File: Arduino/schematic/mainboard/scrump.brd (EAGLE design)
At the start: 100 x 80 mm, 26 parts, among them J1 PINHEAD-FTSH, J2 USB-CON-5PIN-105017-0001, U1 ATSAMD21G-A, U2 LM3671, U3 MCP73831, Y1 32.768kHz

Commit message: Fixed issues after review - Missing 3.3V line on Vddana - Added decoupling cap for second vddio - Removed pull-up on swdclk, which is usually included in the programmer itself. - Added 22 ohm resistor in series with D+ and D-(USB) - Pin 9 of the SWD header is also GND
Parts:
- added C13: 0.1uF, SparkFun-Capacitors:0603-CAP
- added R5: 22R, SparkFun-Resistors:0603-RES
- R1: value 1K -> 22R
- moved R1 31.1 mm to (3.81, -7.62)
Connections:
- new net N$9: R1.1, U1.33
- net +3V3: now also C13.1, C2.1, C4.1, U1.6; no longer R1.2
- net D+: now also R5.2; no longer U1.34
- net D-: now also R1.2; no longer U1.33
- net GND: now also C13.2, J1.9
- net N$4: now also R5.1, U1.34; no longer C2.1, C4.1, U1.6
- net SWCLK: no longer R1.1
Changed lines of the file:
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@@
 <element name="C3" library="SparkFun-Capacitors" package="0603-CAP" value="1.0uF" x="22.86" y="11.43"/>
 <element name="C1" library="SparkFun-Capacitors" package="0603-CAP" value="0.1uF" x="10.16" y="16.51"/>
-<element name="R1" library="SparkFun-Resistors" package="0603-RES" value="1K" x="10.16" y="22.86"/>
 <element name="J2" library="mylibrary" package="USB-MICRO-MOLEX-105017-0001" value="USB-CON-5PIN-105017-0001" x="34.29" y="5.08"/>
 <element name="Y1" library="mylibrary" package="ABS25" value="32.768kHz" x="52.07" y="6.35"/>
@@
 <attribute name="PROD_ID" value="DIO-00819" x="54.61" y="19.05" size="1.778" layer="27" display="off"/>
 </element>
+<element name="C13" library="SparkFun-Capacitors" package="0603-CAP" value="0.1uF" x="3.81" y="-3.81"/>
+<element name="R1" library="SparkFun-Resistors" package="0603-RES" value="22R" x="3.81" y="-7.62"/>
+<element name="R5" library="SparkFun-Resistors" package="0603-RES" value="22R" x="3.81" y="-11.43"/>
 </elements>
 <signals>
@@
 <contactref element="U3" pad="2"/>
 <contactref element="R4" pad="1"/>
-<wire x1="44.45" y1="20.828" x2="53.76" y2="27.94" width="0" layer="19" extent="1-1"/>
+<contactref element="C13" pad="2"/>
+<contactref element="J1" pad="9"/>
+<wire x1="46.99" y1="20.828" x2="53.76" y2="27.94" width="0" layer="19" extent="1-1"/>
+<wire x1="44.45" y1="20.828" x2="46.99" y2="20.828" width="0" layer="19" extent="1-1"/>
 <wire x1="43.18" y1="20.828" x2="44.45" y2="20.828" width="0" layer="19" extent="1-1"/>
 <wire x1="36.83" y1="17.7499" x2="43.18" y2="20.828" width="0" layer="19" extent="1-1"/>
@@
 <wire x1="8.47" y1="2.54" x2="16.09" y2="2.54" width="0" layer="19" extent="1-1"/>
 <wire x1="8.47" y1="7.62" x2="8.47" y2="2.54" width="0" layer="19" extent="1-1"/>
+<wire x1="4.66" y1="-3.81" x2="8.47" y2="2.54" width="0" layer="19" extent="1-1"/>
 <wire x1="45.3" y1="12.7" x2="44.45" y2="20.828" width="0" layer="19" extent="1-1"/>
 <wire x1="42.76" y1="34.29" x2="53.76" y2="27.94" width="0" layer="19" extent="1-1"/>
 <wire x1="64.35" y1="10.16" x2="45.3" y2="12.7" width="0" layer="19" extent="1-1"/>
 <wire x1="69.43" y1="11.43" x2="64.35" y2="10.16" width="0" layer="19" extent="1-1"/>
-</signal>
-<signal name="N$4">
-<contactref element="U1" pad="6"/>
-<contactref element="C4" pad="1"/>
-<contactref element="C2" pad="1"/>
-<wire x1="20.74" y1="3.81" x2="14.8" y2="18.03" width="0" layer="19" extent="1-1"/>
-<wire x1="14.39" y1="2.54" x2="20.74" y2="3.81" width="0" layer="19" extent="1-1"/>
 </signal>
 <signal name="SWDIO">
@@
 <signal name="+3V3">
 <contactref element="U1" pad="17"/>
-<contactref element="U1" pad="36"/>
 <contactref element="U1" pad="44"/>
 <contactref element="J1" pad="1"/>
-<contactref element="R1" pad="2"/>
-<contactref element="C5" pad="1"/>
 <contactref element="C1" pad="1"/>
 <contactref element="C12" pad="1"/>
 <contactref element="U2" pad="4"/>
 <contactref element="L1" pad="1"/>
+<contactref element="U1" pad="6"/>
+<contactref element="C4" pad="1"/>
+<contactref element="C2" pad="1"/>
+<contactref element="C13" pad="1"/>
+<contactref element="U1" pad="36"/>
+<contactref element="C5" pad="1"/>
 <wire x1="37.78" y1="14.0001" x2="41.91" y2="20.828" width="0" layer="19" extent="1-1"/>
 <wire x1="43.6" y1="12.7" x2="37.78" y2="14.0001" width="0" layer="19" extent="1-1"/>
@@
 <wire x1="23.3" y1="20.53" x2="30.85" y2="12.7" width="0" layer="19" extent="1-1"/>
 <wire x1="18.3" y1="22.03" x2="23.3" y2="20.53" width="0" layer="19" extent="1-1"/>
-<wire x1="11.01" y1="22.86" x2="18.3" y2="22.03" width="0" layer="19" extent="1-1"/>
-<wire x1="9.31" y1="16.51" x2="11.01" y2="22.86" width="0" layer="19" extent="1-1"/>
-<wire x1="18.3" y1="13.53" x2="18.3" y2="22.03" width="0" layer="19" extent="1-1"/>
-<wire x1="6.77" y1="2.54" x2="9.31" y2="16.51" width="0" layer="19" extent="1-1"/>
+<wire x1="14.8" y1="18.03" x2="18.3" y2="22.03" width="0" layer="19" extent="1-1"/>
+<wire x1="18.3" y1="13.53" x2="14.8" y2="18.03" width="0" layer="19" extent="1-1"/>
+<wire x1="9.31" y1="16.51" x2="14.8" y2="18.03" width="0" layer="19" extent="1-1"/>
+<wire x1="20.74" y1="3.81" x2="18.3" y2="13.53" width="0" layer="19" extent="1-1"/>
+<wire x1="14.39" y1="2.54" x2="20.74" y2="3.81" width="0" layer="19" extent="1-1"/>
+<wire x1="6.77" y1="2.54" x2="14.39" y2="2.54" width="0" layer="19" extent="1-1"/>
+<wire x1="2.96" y1="-3.81" x2="6.77" y2="2.54" width="0" layer="19" extent="1-1"/>
 </signal>
 <signal name="SWCLK">
 <contactref element="U1" pad="45"/>
-<contactref element="R1" pad="1"/>
 <contactref element="J1" pad="4"/>
 <wire x1="17.8" y1="22.03" x2="43.18" y2="24.892" width="0" layer="19" extent="1-1"/>
-<wire x1="9.31" y1="22.86" x2="17.8" y2="22.03" width="0" layer="19" extent="1-1"/>
 </signal>
 <signal name="PA00">
@@
 <signal name="D+">
 <contactref element="J2" pad="3"/>
-<contactref element="U1" pad="34"/>
-<wire x1="23.3" y1="19.53" x2="36.79" y2="5.08" width="0" layer="19" extent="1-1"/>
+<contactref element="R5" pad="2"/>
+<wire x1="4.66" y1="-11.43" x2="36.79" y2="5.08" width="0" layer="19" extent="1-1"/>
 </signal>
 <signal name="D-">
 <contactref element="J2" pad="2"/>
-<contactref element="U1" pad="33"/>
-<wire x1="23.3" y1="19.03" x2="36.14" y2="5.08" width="0" layer="19" extent="1-1"/>
+<contactref element="R1" pad="2"/>
+<wire x1="4.66" y1="-7.62" x2="36.14" y2="5.08" width="0" layer="19" extent="1-1"/>
 </signal>
 <signal name="+5V">
@@
 <wire x1="54.61" y1="18.173" x2="48.68" y2="35.56" width="0" layer="19" extent="1-1"/>
 </signal>
+<signal name="N$4">
+<contactref element="U1" pad="34"/>
+<contactref element="R5" pad="1"/>
+<wire x1="2.96" y1="-11.43" x2="23.3" y2="19.53" width="0" layer="19" extent="1-1"/>
+</signal>
+<signal name="N$9">
+<contactref element="R1" pad="1"/>
+<contactref element="U1" pad="33"/>
+<wire x1="2.96" y1="-7.62" x2="23.3" y2="19.03" width="0" layer="19" extent="1-1"/>
+</signal>
 </signals>

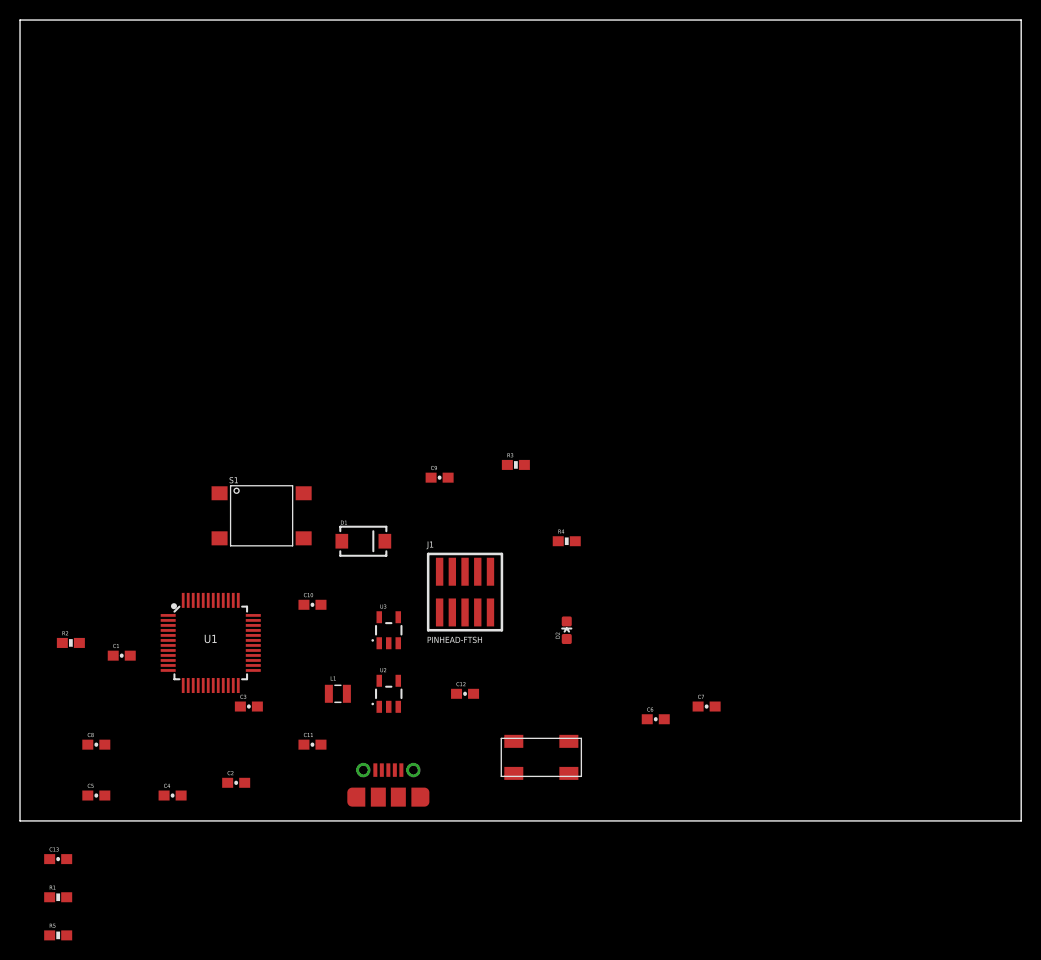
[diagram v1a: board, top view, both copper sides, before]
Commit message: Added DHT11
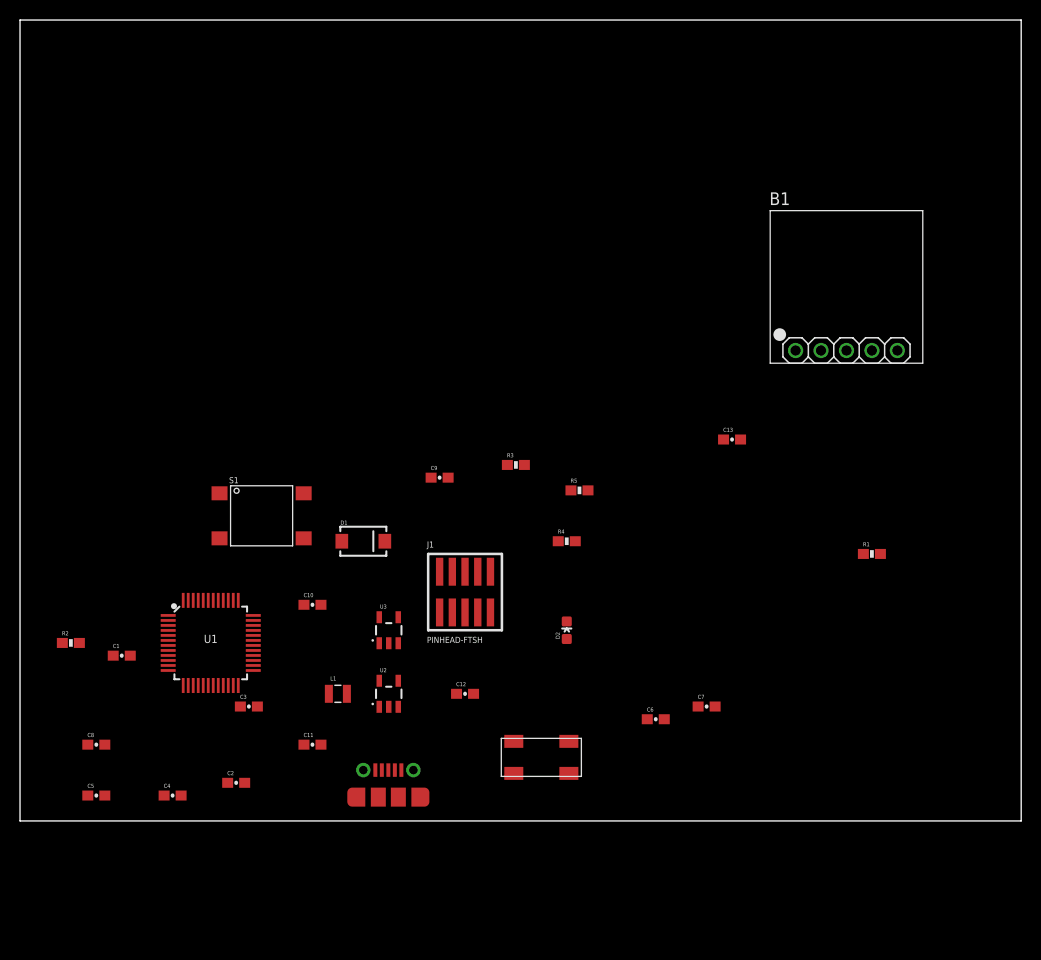
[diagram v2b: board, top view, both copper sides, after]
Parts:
- added B1: BMP180BREAKOUT, mylibrary:BMP180_BREAKOUT
- C6, C7: value 8pF -> 22pF
- moved R1 88.2 mm to (85.1, 26.7)
- moved C13 79.3 mm to (71.1, 38.1)
- moved R5 68.5 mm to (55.9, 33.0)
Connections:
- removed net PA22: U1.31
- removed net PA23: U1.32
- new net SCL: B1.4, U1.32
- new net SDA: B1.5, U1.31
- net +3V3: now also B1.2
- net D+: now also U1.34; no longer J2.3
- net D-: now also U1.33; no longer J2.2
- net GND: now also B1.3
- net N$4: now also J2.3; no longer U1.34
- net N$9: now also J2.2; no longer U1.33
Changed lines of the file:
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@@
 <setting verticaltext="up"/>
 </settings>
-<grid distance="0.05" unitdist="inch" unit="inch" style="lines" multiple="1" display="no" altdistance="0.025" altunitdist="inch" altunit="inch"/>
+<grid distance="0.05" unitdist="inch" unit="mm" style="lines" multiple="1" display="no" altdistance="0.025" altunitdist="inch" altunit="inch"/>
 <layers>
 <layer number="1" name="Top" color="4" fill="1" visible="yes" active="yes"/>
@@
 <element name="J2" library="mylibrary" package="USB-MICRO-MOLEX-105017-0001" value="USB-CON-5PIN-105017-0001" x="34.29" y="5.08"/>
 <element name="Y1" library="mylibrary" package="ABS25" value="32.768kHz" x="52.07" y="6.35"/>
-<element name="C7" library="SparkFun-Capacitors" package="0603-CAP" value="8pF" x="68.58" y="11.43"/>
-<element name="C6" library="SparkFun-Capacitors" package="0603-CAP" value="8pF" x="63.5" y="10.16"/>
+<element name="C7" library="SparkFun-Capacitors" package="0603-CAP" value="22pF" x="68.58" y="11.43"/>
+<element name="C6" library="SparkFun-Capacitors" package="0603-CAP" value="22pF" x="63.5" y="10.16"/>
 <element name="U2" library="mylibrary" package="SOT23-5" value="LM3671" x="36.83" y="12.7"/>
 <element name="C12" library="SparkFun-Capacitors" package="0603-CAP" value="10uF" x="44.45" y="12.7"/>
@@
 <attribute name="PROD_ID" value="DIO-00819" x="54.61" y="19.05" size="1.778" layer="27" display="off"/>
 </element>
-<element name="C13" library="SparkFun-Capacitors" package="0603-CAP" value="0.1uF" x="3.81" y="-3.81"/>
-<element name="R1" library="SparkFun-Resistors" package="0603-RES" value="22R" x="3.81" y="-7.62"/>
-<element name="R5" library="SparkFun-Resistors" package="0603-RES" value="22R" x="3.81" y="-11.43"/>
+<element name="C13" library="SparkFun-Capacitors" package="0603-CAP" value="0.1uF" x="71.12" y="38.1"/>
+<element name="R1" library="SparkFun-Resistors" package="0603-RES" value="22R" x="85.09" y="26.67"/>
+<element name="R5" library="SparkFun-Resistors" package="0603-RES" value="22R" x="55.88" y="33.02"/>
+<element name="B1" library="mylibrary" package="BMP180_BREAKOUT" value="BMP180BREAKOUT" x="74.93" y="45.72"/>
 </elements>
 <signals>
@@
 <contactref element="C13" pad="2"/>
 <contactref element="J1" pad="9"/>
+<contactref element="B1" pad="3"/>
+<wire x1="53.76" y1="27.94" x2="71.97" y2="38.1" width="0" layer="19" extent="1-1"/>
 <wire x1="46.99" y1="20.828" x2="53.76" y2="27.94" width="0" layer="19" extent="1-1"/>
 <wire x1="44.45" y1="20.828" x2="46.99" y2="20.828" width="0" layer="19" extent="1-1"/>
@@
 <wire x1="8.47" y1="2.54" x2="16.09" y2="2.54" width="0" layer="19" extent="1-1"/>
 <wire x1="8.47" y1="7.62" x2="8.47" y2="2.54" width="0" layer="19" extent="1-1"/>
-<wire x1="4.66" y1="-3.81" x2="8.47" y2="2.54" width="0" layer="19" extent="1-1"/>
 <wire x1="45.3" y1="12.7" x2="44.45" y2="20.828" width="0" layer="19" extent="1-1"/>
 <wire x1="42.76" y1="34.29" x2="53.76" y2="27.94" width="0" layer="19" extent="1-1"/>
 <wire x1="64.35" y1="10.16" x2="45.3" y2="12.7" width="0" layer="19" extent="1-1"/>
 <wire x1="69.43" y1="11.43" x2="64.35" y2="10.16" width="0" layer="19" extent="1-1"/>
+<wire x1="82.55" y1="46.99" x2="69.43" y2="11.43" width="0" layer="19" extent="1-1"/>
 </signal>
 <signal name="SWDIO">
@@
 <contactref element="U1" pad="36"/>
 <contactref element="C5" pad="1"/>
+<contactref element="B1" pad="2"/>
+<wire x1="41.91" y1="20.828" x2="70.27" y2="38.1" width="0" layer="19" extent="1-1"/>
 <wire x1="37.78" y1="14.0001" x2="41.91" y2="20.828" width="0" layer="19" extent="1-1"/>
 <wire x1="43.6" y1="12.7" x2="37.78" y2="14.0001" width="0" layer="19" extent="1-1"/>
@@
 <wire x1="14.39" y1="2.54" x2="20.74" y2="3.81" width="0" layer="19" extent="1-1"/>
 <wire x1="6.77" y1="2.54" x2="14.39" y2="2.54" width="0" layer="19" extent="1-1"/>
-<wire x1="2.96" y1="-3.81" x2="6.77" y2="2.54" width="0" layer="19" extent="1-1"/>
+<wire x1="80.01" y1="46.99" x2="70.27" y2="38.1" width="0" layer="19" extent="1-1"/>
 </signal>
 <signal name="SWCLK">
@@
 <contactref element="U1" pad="30"/>
 </signal>
-<signal name="PA22">
+<signal name="SDA">
 <contactref element="U1" pad="31"/>
-</signal>
-<signal name="PA23">
+<contactref element="B1" pad="5"/>
+<wire x1="23.3" y1="18.03" x2="87.63" y2="46.99" width="0" layer="19" extent="1-1"/>
+</signal>
+<signal name="SCL">
 <contactref element="U1" pad="32"/>
+<contactref element="B1" pad="4"/>
+<wire x1="23.3" y1="18.53" x2="85.09" y2="46.99" width="0" layer="19" extent="1-1"/>
 </signal>
 <signal name="PA27">
@@
 </signal>
 <signal name="D+">
-<contactref element="J2" pad="3"/>
 <contactref element="R5" pad="2"/>
-<wire x1="4.66" y1="-11.43" x2="36.79" y2="5.08" width="0" layer="19" extent="1-1"/>
+<contactref element="U1" pad="34"/>
+<wire x1="23.3" y1="19.53" x2="56.73" y2="33.02" width="0" layer="19" extent="1-1"/>
 </signal>
 <signal name="D-">
-<contactref element="J2" pad="2"/>
 <contactref element="R1" pad="2"/>
-<wire x1="4.66" y1="-7.62" x2="36.14" y2="5.08" width="0" layer="19" extent="1-1"/>
+<contactref element="U1" pad="33"/>
+<wire x1="23.3" y1="19.03" x2="85.94" y2="26.67" width="0" layer="19" extent="1-1"/>
 </signal>
 <signal name="+5V">
@@
 </signal>
 <signal name="N$4">
-<contactref element="U1" pad="34"/>
+<contactref element="J2" pad="3"/>
 <contactref element="R5" pad="1"/>
-<wire x1="2.96" y1="-11.43" x2="23.3" y2="19.53" width="0" layer="19" extent="1-1"/>
+<wire x1="36.79" y1="5.08" x2="55.03" y2="33.02" width="0" layer="19" extent="1-1"/>
 </signal>
 <signal name="N$9">
+<contactref element="J2" pad="2"/>
 <contactref element="R1" pad="1"/>
-<contactref element="U1" pad="33"/>
-<wire x1="2.96" y1="-7.62" x2="23.3" y2="19.03" width="0" layer="19" extent="1-1"/>
+<wire x1="36.14" y1="5.08" x2="84.24" y2="26.67" width="0" layer="19" extent="1-1"/>
 </signal>
 </signals>
